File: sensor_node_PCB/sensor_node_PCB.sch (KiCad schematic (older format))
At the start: 16 parts

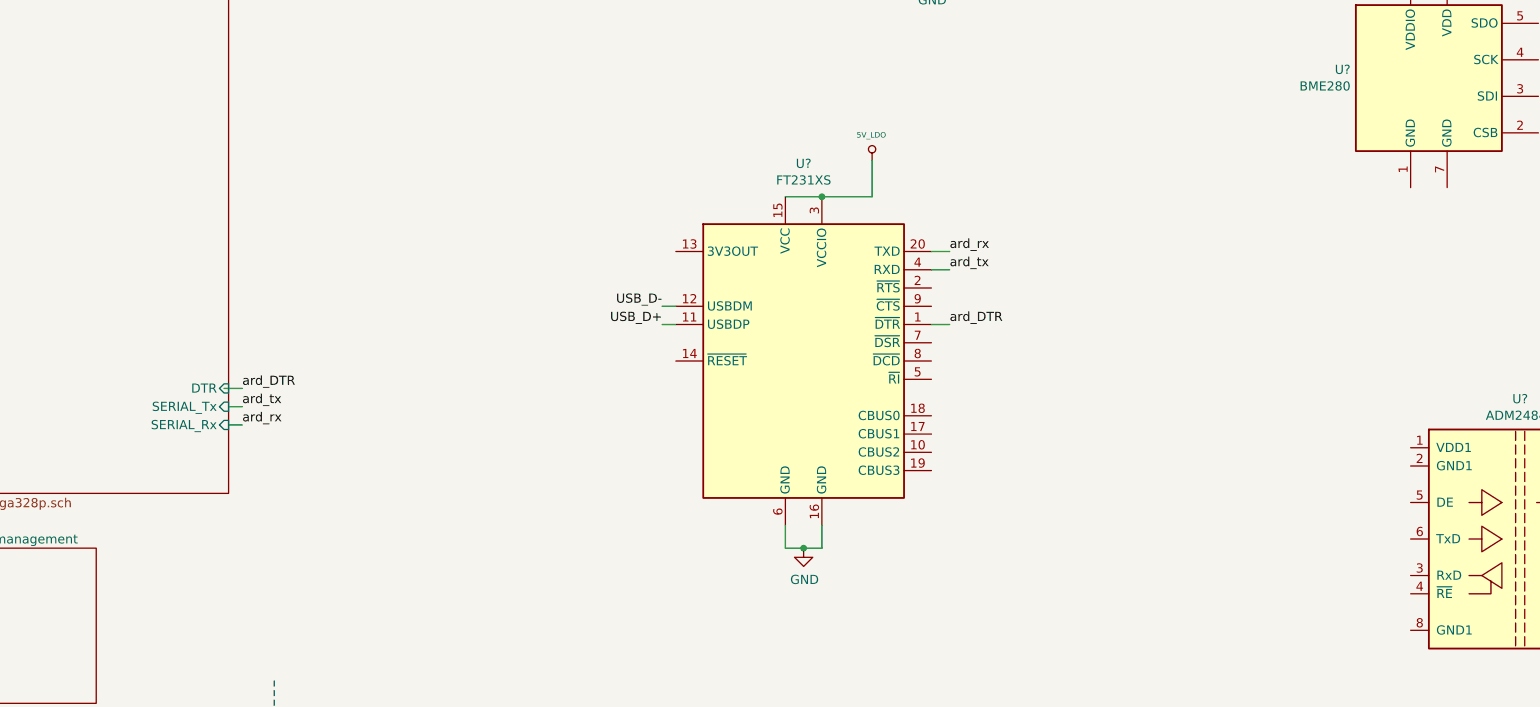
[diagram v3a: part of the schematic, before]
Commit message: changed rs485 transceiver to sp485e
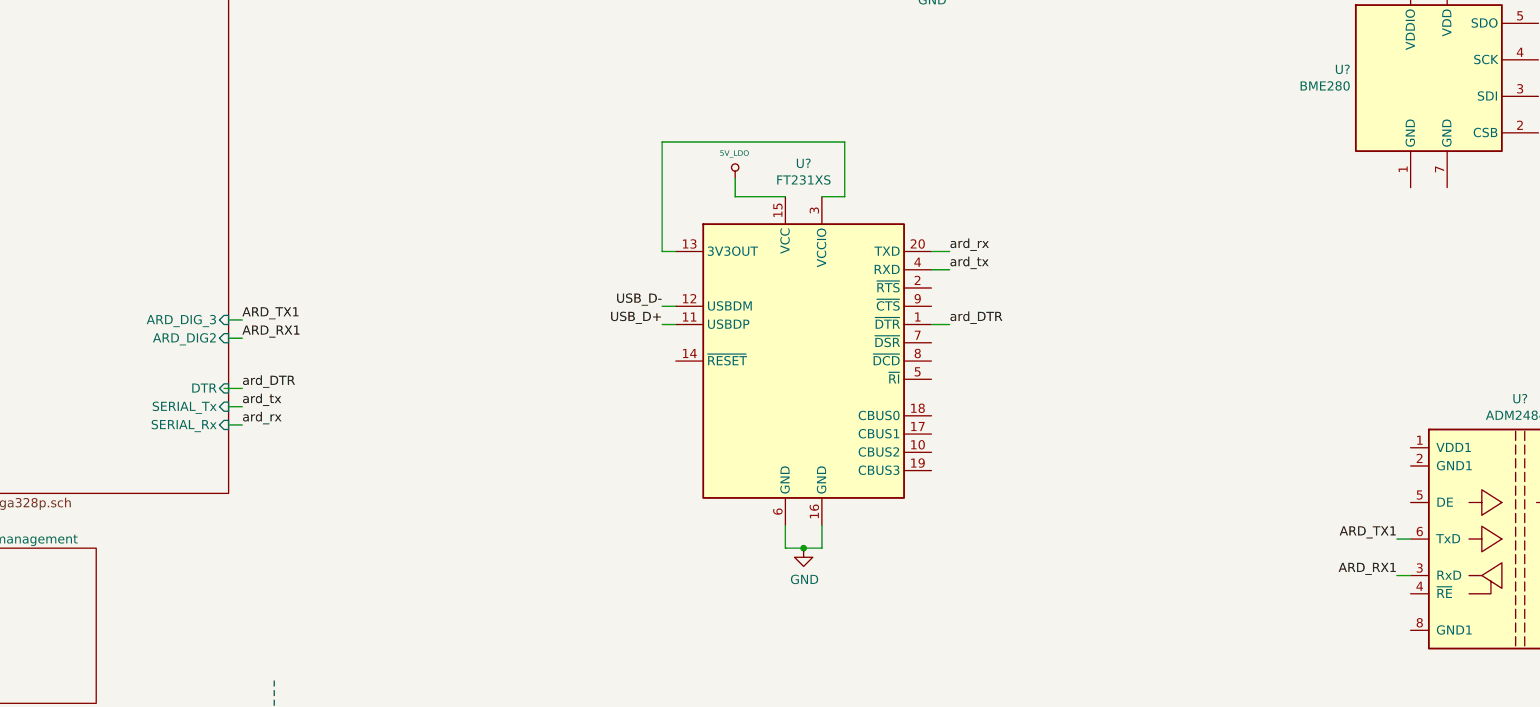
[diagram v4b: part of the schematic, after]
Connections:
- net 5V_LDO: no longer U?.3 (VCCIO)
- net at U?.13 (3V3OUT): now also U?.3 (VCCIO)
- net ARD_RX1: now reaches U?.3 (RxD)
- net ARD_TX1: now reaches U?.6 (TxD)
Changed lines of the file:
@@
 F3 "SERIAL_Tx" I R 2225 4150 50
 F4 "DTR" I R 2225 4050 50
+F5 "ARD_DIG2" I R 2225 3775 50
+F6 "ARD_DIG_3" I R 2225 3675 50
 $EndSheet
 $Sheet
@@
 Wire Wire Line
 	4600 3700 4675 3700
-Wire Wire Line
-	5275 3000 5475 3000
-Wire Wire Line
-	5475 3000 5750 3000
-Wire Wire Line
-	5750 3000 5750 2800
-Connection ~ 5475 3000
 $Comp
 L Arduino_Uno_R3_From_Scratch-rescue:5V_LDO #PWR?
 U 1 1 5F4ED2A9
-P 5750 2800
-F 0 "#PWR?" H 5750 2890 20  0001 C CNN
-F 1 "5V_LDO" H 5746 2938 30  0000 C CNN
-F 2 "" H 5750 2800 60  0000 C CNN
-F 3 "" H 5750 2800 60  0000 C CNN
-	1    5750 2800
+P 5000 2900
+F 0 "#PWR?" H 5000 2990 20  0001 C CNN
+F 1 "5V_LDO" H 4996 3038 30  0000 C CNN
+F 2 "" H 5000 2900 60  0000 C CNN
+F 3 "" H 5000 2900 60  0000 C CNN
+	1    5000 2900
 	1    0    0    -1
 $EndComp
@@
 	5475 4925 5375 4925
 Connection ~ 5375 4925
+Wire Wire Line
+	5000 2900 5000 3000
+Wire Wire Line
+	5000 3000 5275 3000
+Wire Wire Line
+	4675 3300 4600 3300
+Wire Wire Line
+	4600 3300 4600 2700
+Wire Wire Line
+	4600 2700 5600 2700
+Wire Wire Line
+	5600 2700 5600 3000
+Wire Wire Line
+	5600 3000 5475 3000
+Text Label 2300 3675 0    50   ~ 0
+ARD_TX1
+Text Label 2300 3775 0    50   ~ 0
+ARD_RX1
+Wire Wire Line
+	2225 3775 2300 3775
+Wire Wire Line
+	2225 3675 2300 3675
+Text Label 8625 4875 2    50   ~ 0
+ARD_TX1
+Text Label 8625 5075 2    50   ~ 0
+ARD_RX1
+Wire Wire Line
+	8625 4875 8700 4875
+Wire Wire Line
+	8625 5075 8700 5075
 $EndSCHEMATC

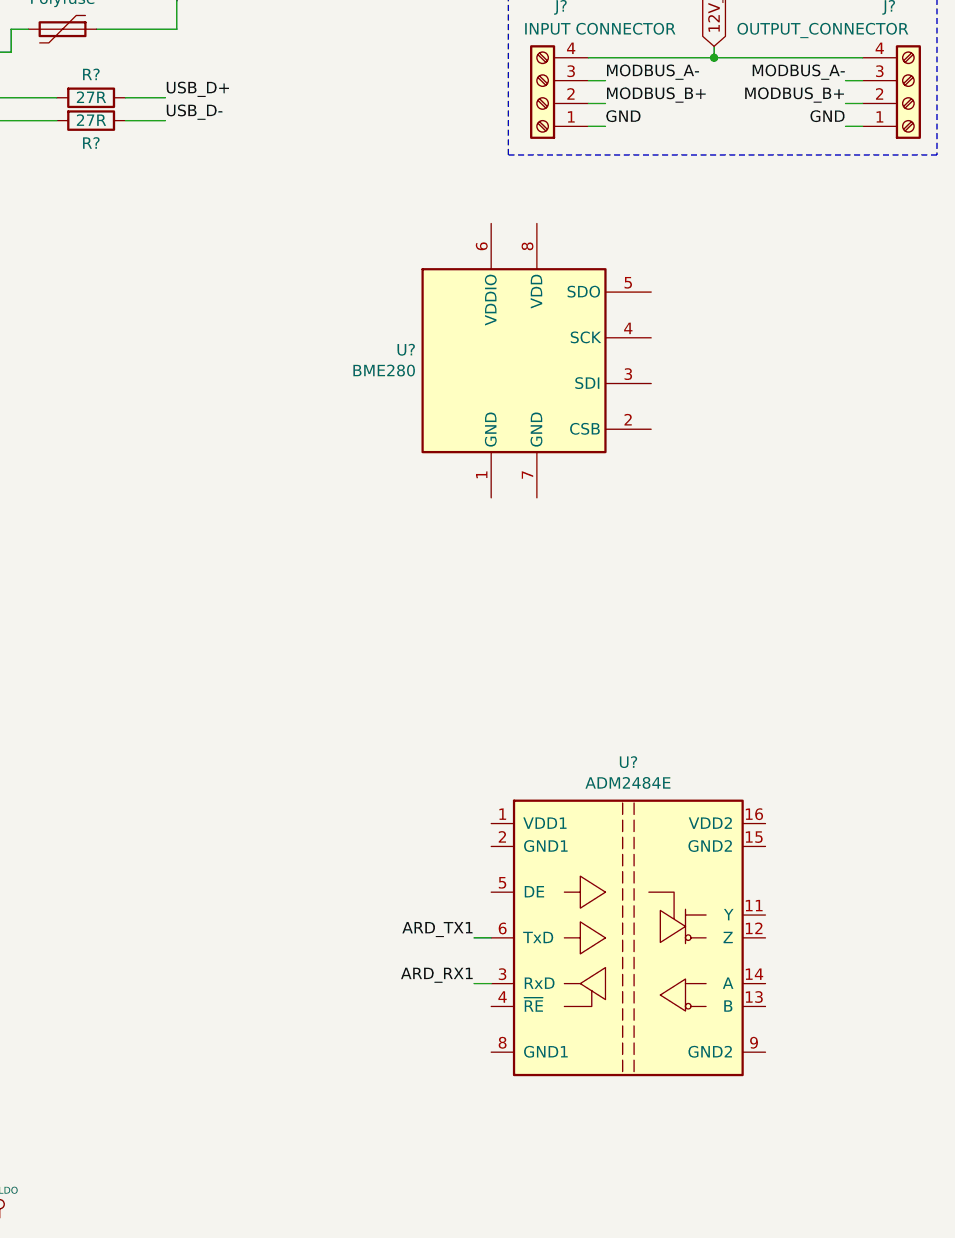
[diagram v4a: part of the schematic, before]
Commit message: started bme280 wiring
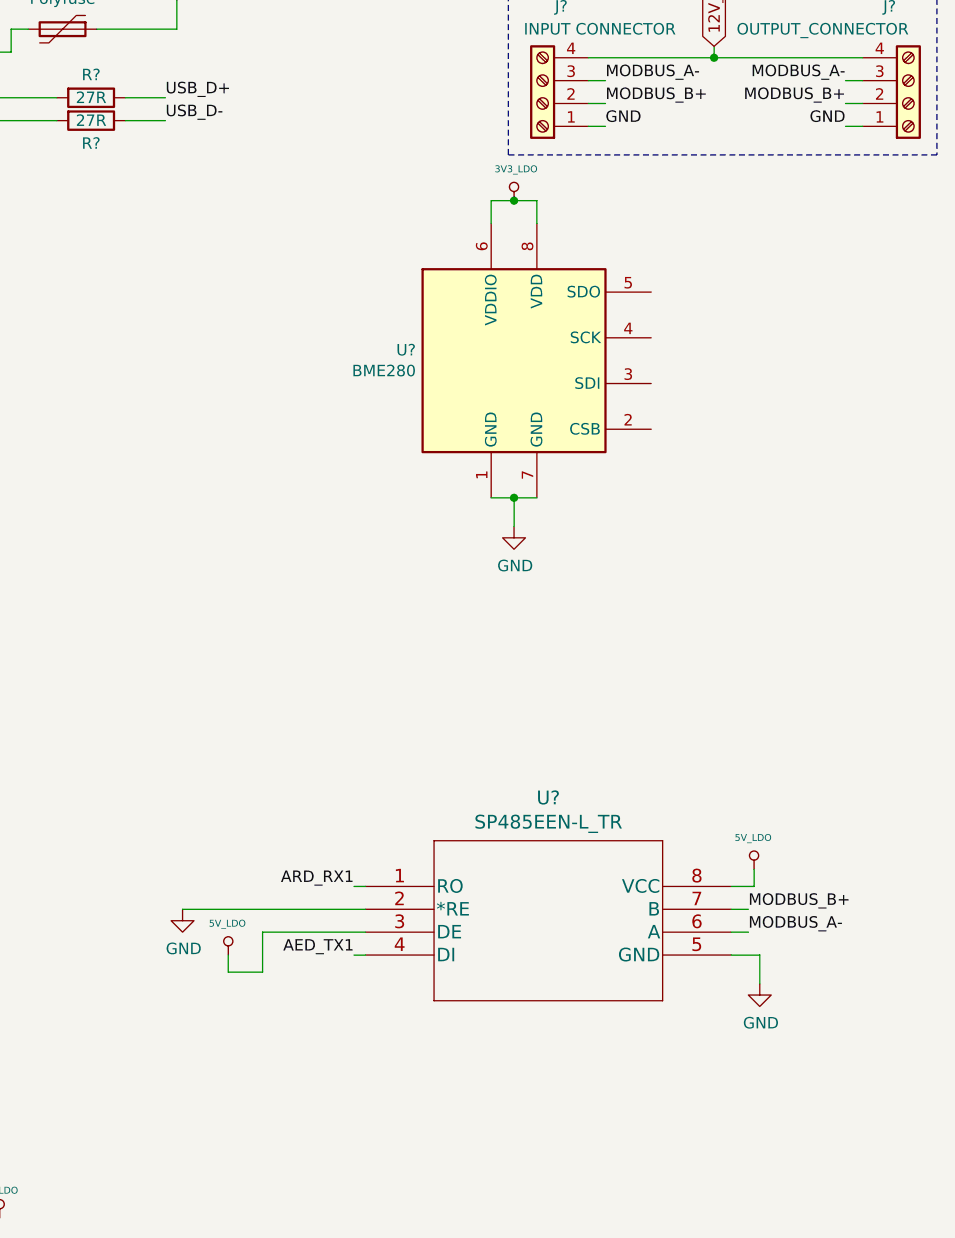
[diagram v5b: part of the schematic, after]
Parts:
- removed U?: ADM2484E, Package_SO:SOIC-16W_7.5x10.3mm_P1.27mm, symbol Interface_UART:ADM2484E
- added U?: SP485EEN-L_TR, NSOIC-8, symbol Kicad_symbols:SP485EEN-L_TR
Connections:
- net 5V_LDO: now also U?.3 (DE), U?.8 (VCC)
- net ARD_RX1: now also U?.1 (RO)
- net GND: now also U?.1 (GND), U?.7 (GND), U?.2 (*RE), U?.5 (GND)
- net MODBUS_A-: now also U?.6 (A)
- net MODBUS_B+: now also U?.7 (B)
- net 3V3_LDO: now reaches U?.6 (VDDIO)
- net 3V3_LDO: now also U?.8 (VDD)
- new net AED_TX1: U?.4 (DI)
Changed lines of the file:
@@
 	9675 1025 10325 1025
-$Comp
-L Interface_UART:ADM2484E U?
-U 1 1 5F4FCE90
-P 9300 4875
-F 0 "U?" H 9300 5642 50  0000 C CNN
-F 1 "ADM2484E" H 9300 5551 50  0000 C CNN
-F 2 "Package_SO:SOIC-16W_7.5x10.3mm_P1.27mm" H 9300 4175 50  0001 C CNN
-F 3 "https://www.analog.com/media/en/technical-documentation/data-sheets/ADM2484E.pdf" H 8550 4925 50  0001 C CNN
-	1    9300 4875
-	1    0    0    -1
-$EndComp
 $Comp
 L Arduino_Uno_R3_From_Scratch-rescue:D D?
@@
 Wire Wire Line
 	2225 3675 2300 3675
-Text Label 8625 4875 2    50   ~ 0
-ARD_TX1
-Text Label 8625 5075 2    50   ~ 0
+$Comp
+L Kicad_symbols:SP485EEN-L_TR U?
+U 1 1 5F4FEF6B
+P 8150 4650
+F 0 "U?" H 8950 5037 60  0000 C CNN
+F 1 "SP485EEN-L_TR" H 8950 4931 60  0000 C CNN
+F 2 "NSOIC-8" H 8950 4890 60  0001 C CNN
+F 3 "" H 8150 4650 60  0000 C CNN
+	1    8150 4650
+	1    0    0    -1
+$EndComp
+Text Label 8100 4950 2    50   ~ 0
+AED_TX1
+Text Label 8100 4650 2    50   ~ 0
 ARD_RX1
 Wire Wire Line
-	8625 4875 8700 4875
-Wire Wire Line
-	8625 5075 8700 5075
+	8100 4650 8150 4650
+Wire Wire Line
+	8100 4950 8150 4950
+$Comp
+L Arduino_Uno_R3_From_Scratch-rescue:GND #PWR?
+U 1 1 5F505092
+P 7350 4750
+F 0 "#PWR?" H 7350 4500 50  0001 C CNN
+F 1 "GND" H 7355 4577 50  0000 C CNN
+F 2 "" H 7350 4750 60  0000 C CNN
+F 3 "" H 7350 4750 60  0000 C CNN
+	1    7350 4750
+	1    0    0    -1
+$EndComp
+Wire Wire Line
+	7350 4750 8150 4750
+$Comp
+L Arduino_Uno_R3_From_Scratch-rescue:GND #PWR?
+U 1 1 5F506F96
+P 9875 5075
+F 0 "#PWR?" H 9875 4825 50  0001 C CNN
+F 1 "GND" H 9880 4902 50  0000 C CNN
+F 2 "" H 9875 5075 60  0000 C CNN
+F 3 "" H 9875 5075 60  0000 C CNN
+	1    9875 5075
+	1    0    0    -1
+$EndComp
+Wire Wire Line
+	9750 4950 9875 4950
+Wire Wire Line
+	9875 4950 9875 5075
+$Comp
+L Arduino_Uno_R3_From_Scratch-rescue:5V_LDO #PWR?
+U 1 1 5F508F61
+P 7550 4950
+F 0 "#PWR?" H 7550 5040 20  0001 C CNN
+F 1 "5V_LDO" H 7546 5088 30  0000 C CNN
+F 2 "" H 7550 4950 60  0000 C CNN
+F 3 "" H 7550 4950 60  0000 C CNN
+	1    7550 4950
+	1    0    0    -1
+$EndComp
+Wire Wire Line
+	8150 4850 7700 4850
+Wire Wire Line
+	7700 4850 7700 5025
+Wire Wire Line
+	7700 5025 7550 5025
+Wire Wire Line
+	7550 5025 7550 4950
+$Comp
+L Arduino_Uno_R3_From_Scratch-rescue:5V_LDO #PWR?
+U 1 1 5F50B3E1
+P 9850 4575
+F 0 "#PWR?" H 9850 4665 20  0001 C CNN
+F 1 "5V_LDO" H 9846 4713 30  0000 C CNN
+F 2 "" H 9850 4575 60  0000 C CNN
+F 3 "" H 9850 4575 60  0000 C CNN
+	1    9850 4575
+	1    0    0    -1
+$EndComp
+Wire Wire Line
+	9850 4650 9850 4575
+Wire Wire Line
+	9750 4650 9850 4650
+Text Label 9825 4850 0    50   ~ 0
+MODBUS_A-
+Text Label 9825 4750 0    50   ~ 0
+MODBUS_B+
+Wire Wire Line
+	9750 4750 9825 4750
+Wire Wire Line
+	9750 4850 9825 4850
+$Comp
+L Arduino_Uno_R3_From_Scratch-rescue:GND #PWR?
+U 1 1 5F51E415
+P 8800 3075
+F 0 "#PWR?" H 8800 2825 50  0001 C CNN
+F 1 "GND" H 8805 2902 50  0000 C CNN
+F 2 "" H 8800 3075 60  0000 C CNN
+F 3 "" H 8800 3075 60  0000 C CNN
+	1    8800 3075
+	1    0    0    -1
+$EndComp
+Wire Wire Line
+	8700 2950 8800 2950
+Wire Wire Line
+	8800 2950 8800 3075
+Connection ~ 8800 2950
+Wire Wire Line
+	8800 2950 8900 2950
+$Comp
+L Arduino_Uno_R3_From_Scratch-rescue:3V3_LDO #PWR?
+U 1 1 5F522D75
+P 8800 1650
+F 0 "#PWR?" H 8800 1610 30  0001 C CNN
+F 1 "3V3_LDO" H 8809 1788 30  0000 C CNN
+F 2 "" H 8800 1650 60  0000 C CNN
+F 3 "" H 8800 1650 60  0000 C CNN
+	1    8800 1650
+	1    0    0    -1
+$EndComp
+Wire Wire Line
+	8700 1750 8700 1650
+Wire Wire Line
+	8700 1650 8800 1650
+Wire Wire Line
+	8900 1750 8900 1650
+Wire Wire Line
+	8900 1650 8800 1650
+Connection ~ 8800 1650
 $EndSCHEMATC

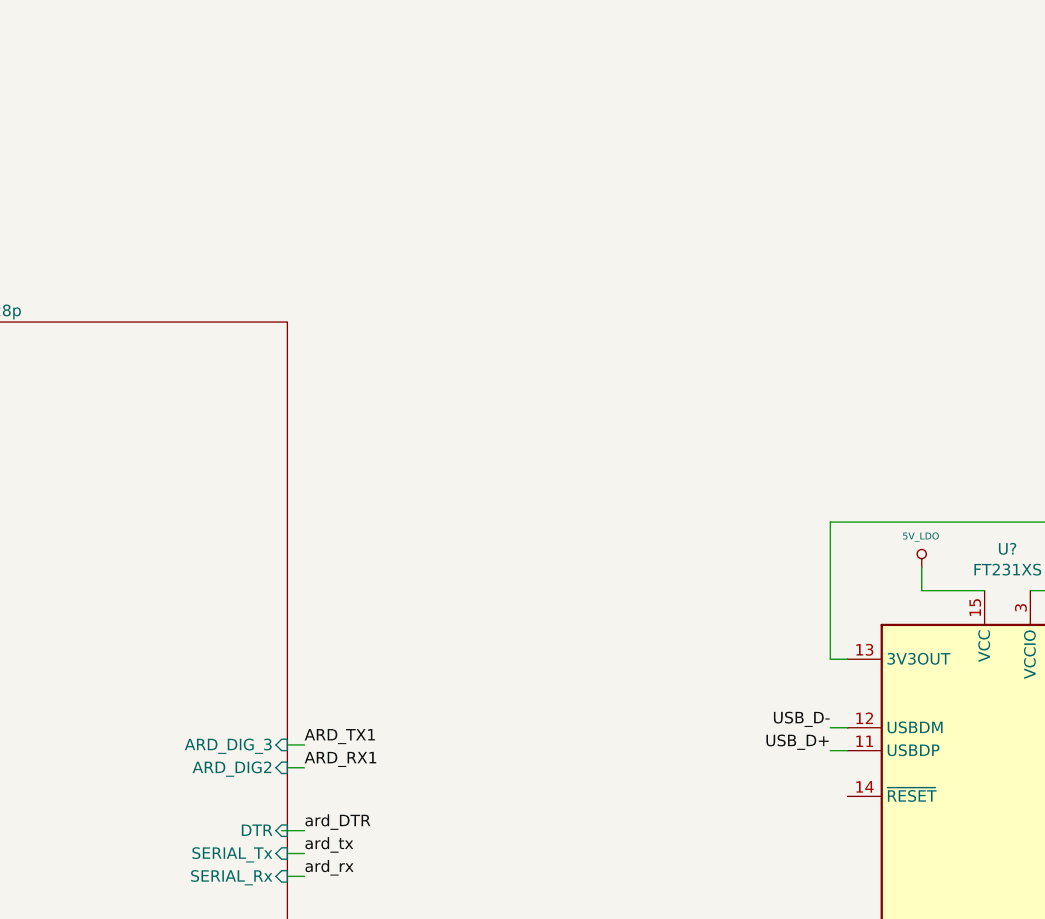
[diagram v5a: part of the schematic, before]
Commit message: added sensair s8
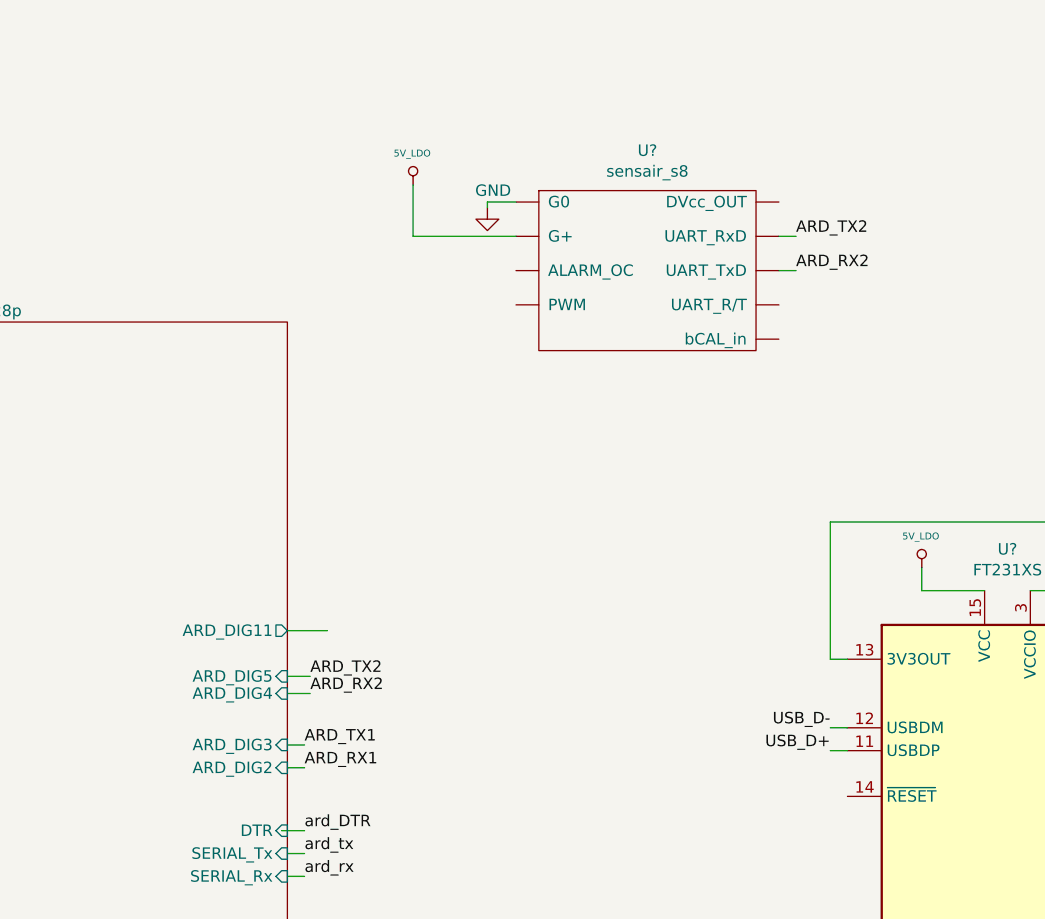
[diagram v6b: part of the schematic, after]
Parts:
- added U?: sensair_s8, symbol Kicad_symbols:sensair_s8
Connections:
- net 5V_LDO: now also U?.~ (UART_TxD)
- net GND: now also U?.~ (UART_TxD)
- new net ARD_RX2: U?.~ (UART_TxD)
- new net ARD_TX2: U?.~ (UART_TxD)
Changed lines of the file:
@@
 F4 "DTR" I R 2225 4050 50
 F5 "ARD_DIG2" I R 2225 3775 50
-F6 "ARD_DIG_3" I R 2225 3675 50
+F6 "ARD_DIG3" I R 2225 3675 50
+F7 "ARD_DIG4" I R 2225 3450 50
+F8 "ARD_DIG5" I R 2225 3375 50
+F9 "ARD_DIG11" O R 2225 3175 50
 $EndSheet
 $Sheet
@@
 	8900 1650 8800 1650
 Connection ~ 8800 1650
+$Comp
+L Kicad_symbols:sensair_s8 U?
+U 1 1 5F514B72
+P 3775 1500
+F 0 "U?" H 3800 1925 50  0000 C CNN
+F 1 "sensair_s8" H 3800 1834 50  0000 C CNN
+F 2 "" H 3625 1500 50  0001 C CNN
+F 3 "" H 3625 1500 50  0001 C CNN
+	1    3775 1500
+	1    0    0    -1
+$EndComp
+$Comp
+L Arduino_Uno_R3_From_Scratch-rescue:5V_LDO #PWR?
+U 1 1 5F51697E
+P 2775 1225
+F 0 "#PWR?" H 2775 1315 20  0001 C CNN
+F 1 "5V_LDO" H 2771 1363 30  0000 C CNN
+F 2 "" H 2775 1225 60  0000 C CNN
+F 3 "" H 2775 1225 60  0000 C CNN
+	1    2775 1225
+	1    0    0    -1
+$EndComp
+Wire Wire Line
+	2775 1225 2775 1450
+Wire Wire Line
+	2775 1450 3225 1450
+$Comp
+L Arduino_Uno_R3_From_Scratch-rescue:GND #PWR?
+U 1 1 5F5191A0
+P 3100 1325
+F 0 "#PWR?" H 3100 1075 50  0001 C CNN
+F 1 "GND" H 3125 1400 50  0000 C CNN
+F 2 "" H 3100 1325 60  0000 C CNN
+F 3 "" H 3100 1325 60  0000 C CNN
+	1    3100 1325
+	1    0    0    -1
+$EndComp
+Wire Wire Line
+	3100 1325 3100 1300
+Wire Wire Line
+	3100 1300 3225 1300
+Text Label 2325 3375 0    50   ~ 0
+ARD_TX2
+Wire Wire Line
+	2225 3375 2325 3375
+Text Label 2325 3450 0    50   ~ 0
+ARD_RX2
+Wire Wire Line
+	2225 3450 2325 3450
+Text Label 4450 1600 0    50   ~ 0
+ARD_RX2
+Text Label 4450 1450 0    50   ~ 0
+ARD_TX2
+Wire Wire Line
+	4375 1450 4450 1450
+Wire Wire Line
+	4375 1600 4450 1600
+Wire Wire Line
+	2225 3175 2400 3175
 $EndSCHEMATC
